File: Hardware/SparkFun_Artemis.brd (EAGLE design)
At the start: 15 x 10 mm, 65 parts, among them J1 PAD, J10 PAD, J11 PAD, J12 PAD, J13 PAD, J14 PAD, J15 PAD, J16 PAD, J17 PAD, J18 PAD, J19 PAD, J2 PAD, J20 PAD, J21 PAD, J22 PAD, J23 PAD, J24 PAD, J25 PAD, J26 PAD, J27 PAD, J28 PAD, J29 PAD, J3 PAD, J30 PAD, J31 PAD, J32 PAD, J33 PAD, J34 PAD, J35 PAD, J36 PAD, J37 PAD, J38 PAD, J39 PAD, J4 PAD, J40 PAD, J5 PAD, J6 PAD, J7 PAD, J8 PAD, J9 PAD, U1 AMBIQ-APOLLO3KBR, Y1 32MHz

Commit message: Moar pins
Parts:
- added J41, J42, J43: PAD, Module-Pads:MODULE_PAD
- moved J35 8.34 mm to (9.50, 0.50), turned to 90 degrees
- moved J39 8.34 mm to (11.0, 1.30)
- moved J37 8.22 mm to (10.0, 1.30), turned to 90 degrees
- moved J38 8.22 mm to (10.5, 0.50), turned to 90 degrees
- moved J22 2.00 mm to (9.50, 9.50)
- moved J23 2.00 mm to (10.5, 9.50)
- moved J3 2.00 mm to (8.50, 9.50)
- moved J31 2.00 mm to (7.50, 9.50)
- moved J19 1.00 mm to (5.50, 9.50)
- moved J21 1.00 mm to (9.00, 8.70)
- moved J32 1.00 mm to (8.00, 8.70)
- moved J36 1.00 mm to (10.0, 8.70)
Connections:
- new net D10: J43.1, U1.G8
- new net D8: J42.1, U1.F8
- new net ~D4: J41.1, U1.D9
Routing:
- net D36: track 3.56 -> 9.28 mm
- net ~D37: track 3.59 -> 9.02 mm
- net ~SDA3/MISO3: track 4.14 -> 7.46 mm
- net ~SCL3/SCK3: track 4.98 -> 8.27 mm
- net D8: track 0.00 -> 1.55 mm, vias 0 -> 1
- net ~D4: track 0.00 -> 1.54 mm, vias 0 -> 1
- net ~D44: track 2.26 -> 3.74 mm
- net GND: track 13.5 -> 15.0 mm
- net MOSI: track 2.63 -> 1.37 mm
- net MOSI3: track 2.16 -> 3.11 mm
- net SDA: track 1.16 -> 2.06 mm
- net D10: track 0.00 -> 0.75 mm, vias 0 -> 1
- net SCL: track 0.75 -> 1.40 mm
- net TXO-0: track 1.81 -> 1.30 mm

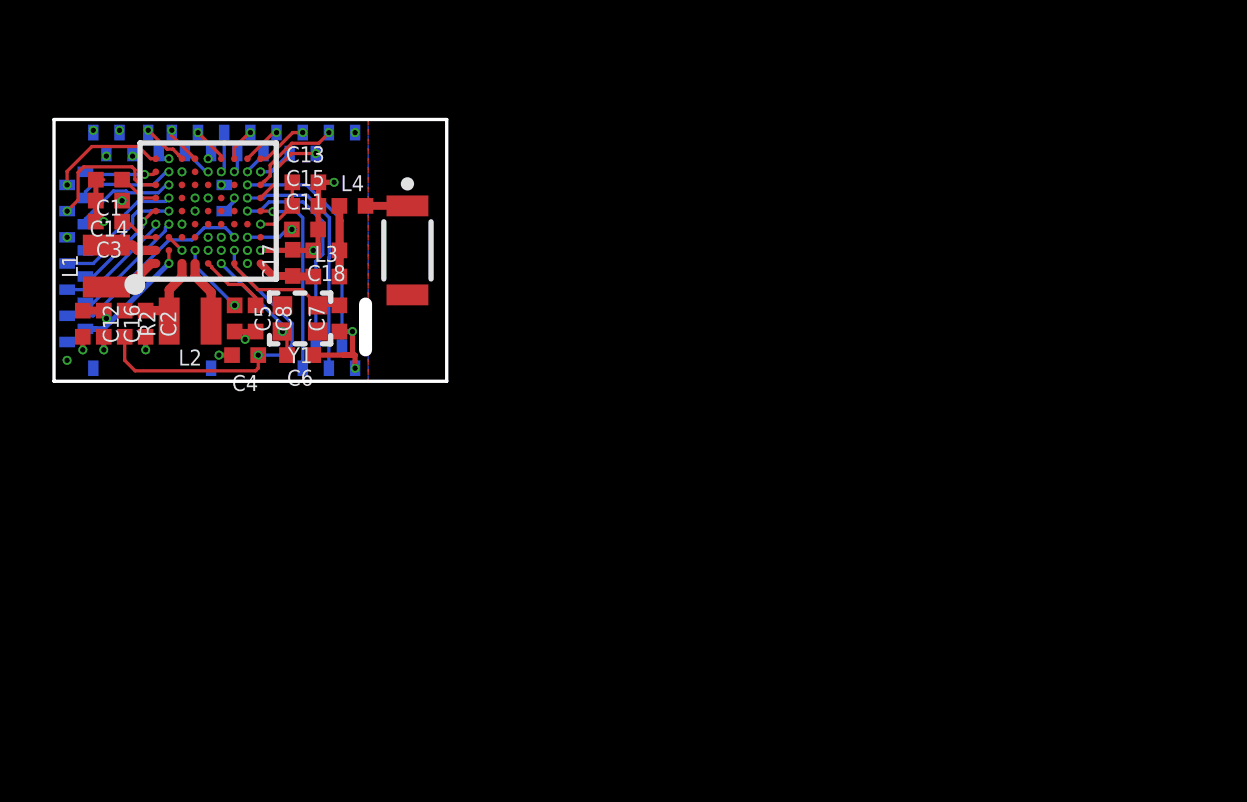
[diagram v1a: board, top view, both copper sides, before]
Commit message: Add C9 pad. Add FP for Artemis module.
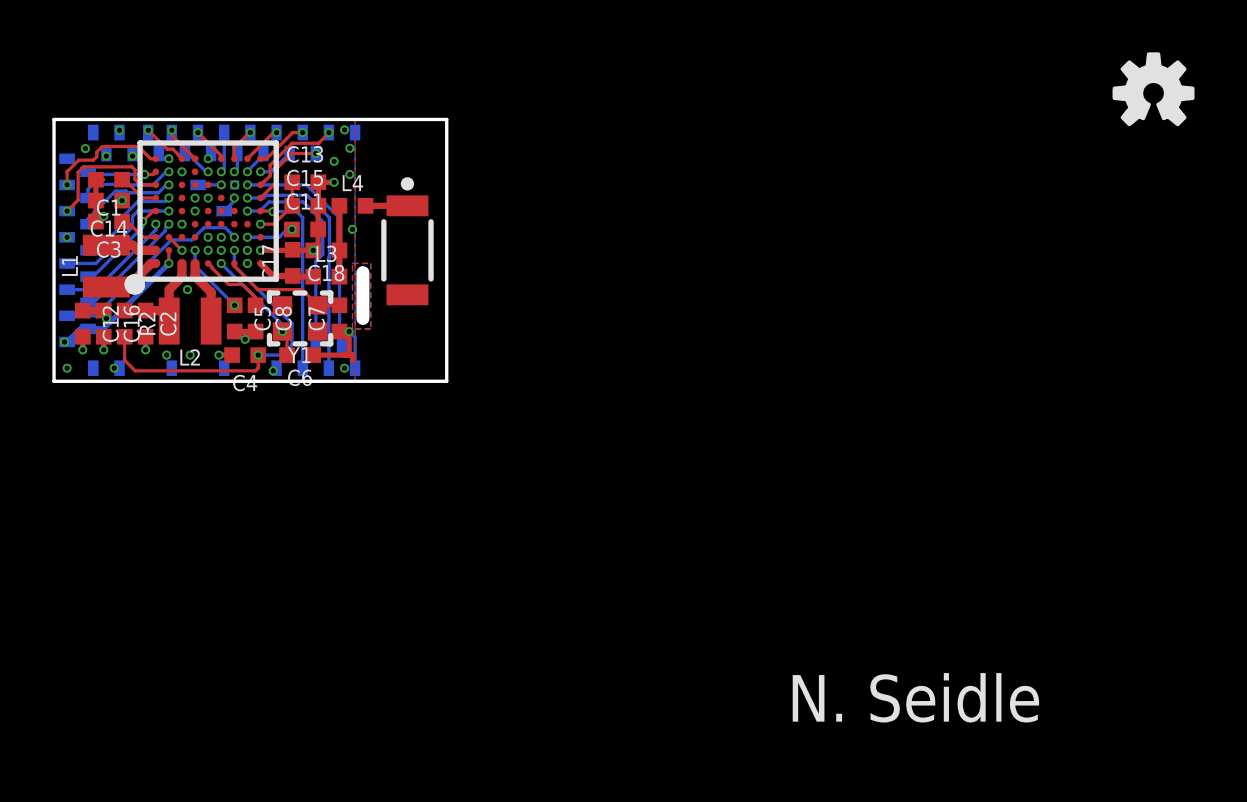
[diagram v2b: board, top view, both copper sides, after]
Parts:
- added J44, J45, J47, J48: PAD.4X.6, Module-Pads:MODULE_PAD
- added J46: PAD.35X.35, Module-Pads:MODULE_MINI_PAD
- added LOGO1: SFE_LOGO_FLAME.05_INCH_INTERNAL, SparkFun-Aesthetics:SFE_LOGO_FLAME_INTERNAL_0.05
- added LOGO2: OSHW-LOGOS, SparkFun-Aesthetics:OSHW-LOGO-S
- J1, J10, J11, J12, J13, J14, J15, J16, J17, J18, J19, J2, J20, J21, J22, J23, J24, J25, J26, J27, J28, J29, J3, J30, J31, J32, J34, J35, J36, J37, J38, J39, J4, J40, J41, J42, J43, J49, J5, J6, J7, J8, J9: value PAD -> PAD.4X.6
- moved J1 1.00 mm to (5.50, 7.50)
- moved J34 0.50 mm to (6.50, 0.50)
- moved J12 0.10 mm to (1.30, 8.00)
- moved J13 0.10 mm to (1.30, 7.00)
- moved J15 0.10 mm to (1.30, 4.00)
- moved J28 0.10 mm to (1.30, 5.00)
- moved J29 0.10 mm to (1.30, 2.00)
- moved J7 0.10 mm to (1.30, 6.00)
- moved J9 0.10 mm to (1.30, 3.00)
- turned J49 to 0 degrees
- renumbered J33 to J49
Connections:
- net GPIO33/SWO renamed ~AD33/SWO
- net MOSI renamed D7
- net MOSI3 renamed D38
- net RXI-1 renamed ~D25
- net SCL renamed ~D39
- net SDA renamed D40
- net TXO-1 renamed ~D24
- net ~AD31/RTS renamed ~AD31
- net ~D10/CTS renamed ~D26
- net ~MISO renamed ~D6
- net ~SCK renamed ~D5
- net ~SCL3/SCK3 renamed ~D42
- net ~SDA3/MISO3 renamed ~D43
- new net D9: J46.1, U1.G7
- net GND: now also J44.1, J45.1, J47.1, J48.1; no longer J49.1
- net VDD: now also J49.1
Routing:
- net VDD: track 8.87 -> 9.78 mm, vias 6 -> 7
- net SWDIO: track 0.11 -> 0.89 mm
- net GND: track 15.0 -> 15.7 mm, vias 20 -> 29
- net D9: track 0.00 -> 0.01 mm, vias 0 -> 1
- added copper zone on layer 1, net N$4
- added copper zone on layer 15, net N$4
- added copper zone on layer 16, net N$4
- added copper zone on layer 2, net N$4
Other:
- outline, holes or cut-outs redrawn
- board text added: "1"
- board text added: "10"
- board text added: "11"
- board text added: "12"
- board text added: "13"
- board text added: "14"
- board text added: "15"
- board text added: "16"
- board text added: "17"
- board text added: "18"
- board text added: "19"
- board text added: "2"
- board text added: "20"
- board text added: "21"
- board text added: "22"
- board text added: "23"
- board text added: "24"
- board text added: "25"
- board text added: "26"
- board text added: "27"
- board text added: "28"
- board text added: "29"
- board text added: "3"
- board text added: "30"
- board text added: "31"
- board text added: "32"
- board text added: "33"
- board text added: "34"
- board text added: "35"
- board text added: "36"
- board text added: "37"
- board text added: "38"
- board text added: "39"
- board text added: "4"
- board text added: "40"
- board text added: "41"
- board text added: "42"
- board text added: "43"
- board text added: "44"
- board text added: "45"
- board text added: "46"
- board text added: "47"
- board text added: "48"
- board text added: "5"
- board text added: "6"
- board text added: "7"
- board text added: "8"
- board text added: "9"
- board text added: "Dimension: mm"
- board text added: "Exposed Copper: 0.5mm"
- board text added: "Milled Slot for alignment leg"
- board text added: "N. Seidle"
- board text added: "RF Shield: H:1.3-1.5mm Long Leg: 1.8-1.9mm"
- board text added: "This is a 4-layer board"
- board text removed: "This is a 4-layer board!"

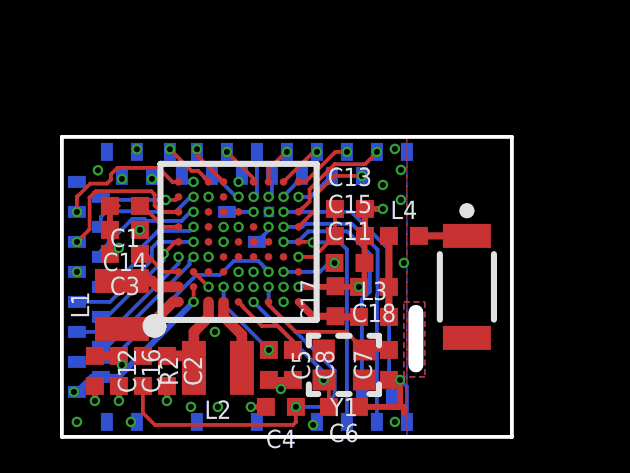
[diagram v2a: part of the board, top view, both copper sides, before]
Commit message: Fix pad slightly off center.
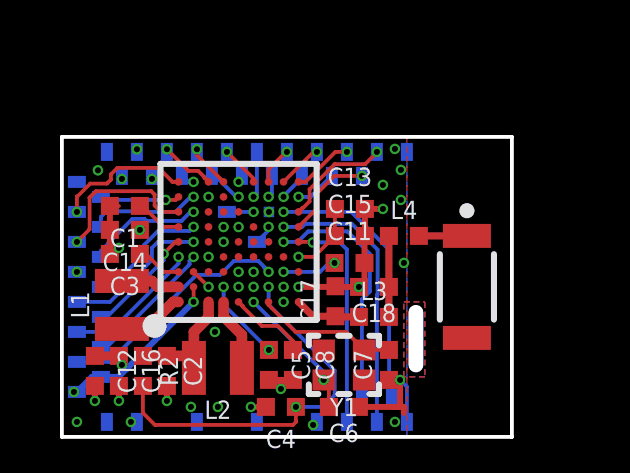
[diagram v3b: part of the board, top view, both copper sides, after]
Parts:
- moved J40 0.10 mm to (3.50, 9.50)
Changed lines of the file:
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@@
 <grid distance="1" unitdist="mm" unit="mm" style="lines" multiple="1" display="yes" altdistance="0.1" altunitdist="mm" altunit="mm"/>
 <layers>
-<layer number="1" name="Top" color="4" fill="1" visible="no" active="yes"/>
-<layer number="16" name="Bottom" color="1" fill="1" visible="no" active="yes"/>
-<layer number="17" name="Pads" color="2" fill="1" visible="no" active="yes"/>
-<layer number="18" name="Vias" color="2" fill="1" visible="no" active="yes"/>
-<layer number="19" name="Unrouted" color="6" fill="1" visible="no" active="yes"/>
-<layer number="20" name="Dimension" color="24" fill="1" visible="no" active="yes"/>
-<layer number="21" name="tPlace" color="16" fill="1" visible="no" active="yes"/>
-<layer number="22" name="bPlace" color="14" fill="1" visible="no" active="yes"/>
-<layer number="23" name="tOrigins" color="15" fill="1" visible="no" active="yes"/>
-<layer number="24" name="bOrigins" color="15" fill="1" visible="no" active="yes"/>
+<layer number="1" name="Top" color="4" fill="1" visible="yes" active="yes"/>
+<layer number="16" name="Bottom" color="1" fill="1" visible="yes" active="yes"/>
+<layer number="17" name="Pads" color="2" fill="1" visible="yes" active="yes"/>
+<layer number="18" name="Vias" color="2" fill="1" visible="yes" active="yes"/>
+<layer number="19" name="Unrouted" color="6" fill="1" visible="yes" active="yes"/>
+<layer number="20" name="Dimension" color="24" fill="1" visible="yes" active="yes"/>
+<layer number="21" name="tPlace" color="16" fill="1" visible="yes" active="yes"/>
+<layer number="22" name="bPlace" color="14" fill="1" visible="yes" active="yes"/>
+<layer number="23" name="tOrigins" color="15" fill="1" visible="yes" active="yes"/>
+<layer number="24" name="bOrigins" color="15" fill="1" visible="yes" active="yes"/>
 <layer number="25" name="tNames" color="7" fill="1" visible="no" active="yes"/>
 <layer number="26" name="bNames" color="7" fill="1" visible="no" active="yes"/>
@@
 <layer number="43" name="vRestrict" color="2" fill="10" visible="no" active="yes"/>
 <layer number="44" name="Drills" color="7" fill="1" visible="no" active="yes"/>
-<layer number="45" name="Holes" color="7" fill="1" visible="no" active="yes"/>
+<layer number="45" name="Holes" color="7" fill="1" visible="yes" active="yes"/>
 <layer number="46" name="Milling" color="3" fill="1" visible="no" active="yes"/>
 <layer number="47" name="Measures" color="7" fill="1" visible="no" active="yes"/>
@@
 <layer number="49" name="Reference" color="7" fill="1" visible="yes" active="yes"/>
 <layer number="50" name="RF_Shield_Dimensions2" color="47" fill="1" visible="no" active="yes"/>
-<layer number="51" name="tDocu" color="6" fill="1" visible="no" active="yes"/>
+<layer number="51" name="tDocu" color="6" fill="1" visible="yes" active="yes"/>
 <layer number="52" name="bDocu" color="7" fill="1" visible="no" active="yes"/>
 <layer number="91" name="Nets" color="2" fill="1" visible="no" active="no"/>
@@
 <rectangle x1="4.3" y1="9.2" x2="4.7" y2="9.8" layer="51" rot="R180"/>
 <rectangle x1="3.8" y1="8.4" x2="4.2" y2="9" layer="51" rot="R180"/>
-<rectangle x1="3.4" y1="9.2" x2="3.8" y2="9.8" layer="51" rot="R180"/>
+<rectangle x1="3.3" y1="9.2" x2="3.7" y2="9.8" layer="51" rot="R180"/>
 <rectangle x1="2.8" y1="8.4" x2="3.2" y2="9" layer="51" rot="R180"/>
 <rectangle x1="2.3" y1="9.2" x2="2.7" y2="9.8" layer="51" rot="R180"/>
@@
 <text x="4.5" y="9.5" size="0.2" layer="49" font="vector" ratio="15" align="center">14</text>
 <text x="4" y="8.7" size="0.2" layer="49" font="vector" ratio="15" align="center">15</text>
-<text x="3.6" y="9.5" size="0.2" layer="49" font="vector" ratio="15" align="center">16</text>
+<text x="3.5" y="9.5" size="0.2" layer="49" font="vector" ratio="15" rot="R180" align="center">16</text>
 <text x="3" y="8.6" size="0.2" layer="49" font="vector" ratio="15" align="center">17</text>
 <text x="2.5" y="9.5" size="0.2" layer="49" font="vector" ratio="15" align="center">18</text>
@@
 <element name="J38" library="Module-Pads" package="MODULE_PAD" value="PAD.4X.6" x="10.5" y="0.5" smashed="yes" rot="MR90"/>
 <element name="J39" library="Module-Pads" package="MODULE_PAD" value="PAD.4X.6" x="11" y="1.3" smashed="yes" rot="MR270"/>
-<element name="J40" library="Module-Pads" package="MODULE_PAD" value="PAD.4X.6" x="3.6" y="9.5" smashed="yes" rot="MR270"/>
+<element name="J40" library="Module-Pads" package="MODULE_PAD" value="PAD.4X.6" x="3.5" y="9.5" smashed="yes" rot="MR270"/>
 <element name="J41" library="Module-Pads" package="MODULE_PAD" value="PAD.4X.6" x="4.5" y="9.5" smashed="yes" rot="MR270"/>
 <element name="J42" library="Module-Pads" package="MODULE_PAD" value="PAD.4X.6" x="6.5" y="9.5" smashed="yes" rot="MR270"/>
@@
 <contactref element="U1" pad="C9"/>
 <contactref element="J40" pad="1"/>
-<via x="3.6" y="9.5884" extent="1-16" drill="0.2"/>
+<via x="3.5" y="9.5884" extent="1-16" drill="0.2"/>
 <wire x1="4.7547" y1="8.65289375" x2="4.53989375" y2="8.8677" width="0.127" layer="1"/>
-<wire x1="4.53989375" y1="8.8677" x2="4.3207" y2="8.8677" width="0.127" layer="1"/>
-<wire x1="4.3207" y1="8.8677" x2="3.6" y2="9.5884" width="0.127" layer="1"/>
+<wire x1="4.53989375" y1="8.8677" x2="4.2207" y2="8.8677" width="0.127" layer="1"/>
+<wire x1="4.2207" y1="8.8677" x2="3.5" y2="9.5884" width="0.127" layer="1"/>
 <wire x1="4.888" y1="8.501" x2="4.7547" y2="8.6343" width="0.127" layer="1"/>
 <wire x1="4.7547" y1="8.6343" x2="4.7547" y2="8.65289375" width="0.127" layer="1"/>
-<wire x1="3.6" y1="9.5884" x2="3.6" y2="9.5" width="0.127" layer="16"/>
+<wire x1="3.5" y1="9.5" x2="3.5" y2="9.5884" width="0.127" layer="16"/>
 </signal>
 <signal name="~D4">
